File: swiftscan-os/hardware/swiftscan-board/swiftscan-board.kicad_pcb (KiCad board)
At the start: 2 copper layers, 80 x 55 mm, 11 parts, among them J1 I2S_MIC, U1 ATECC608A, U2 VCNL4040

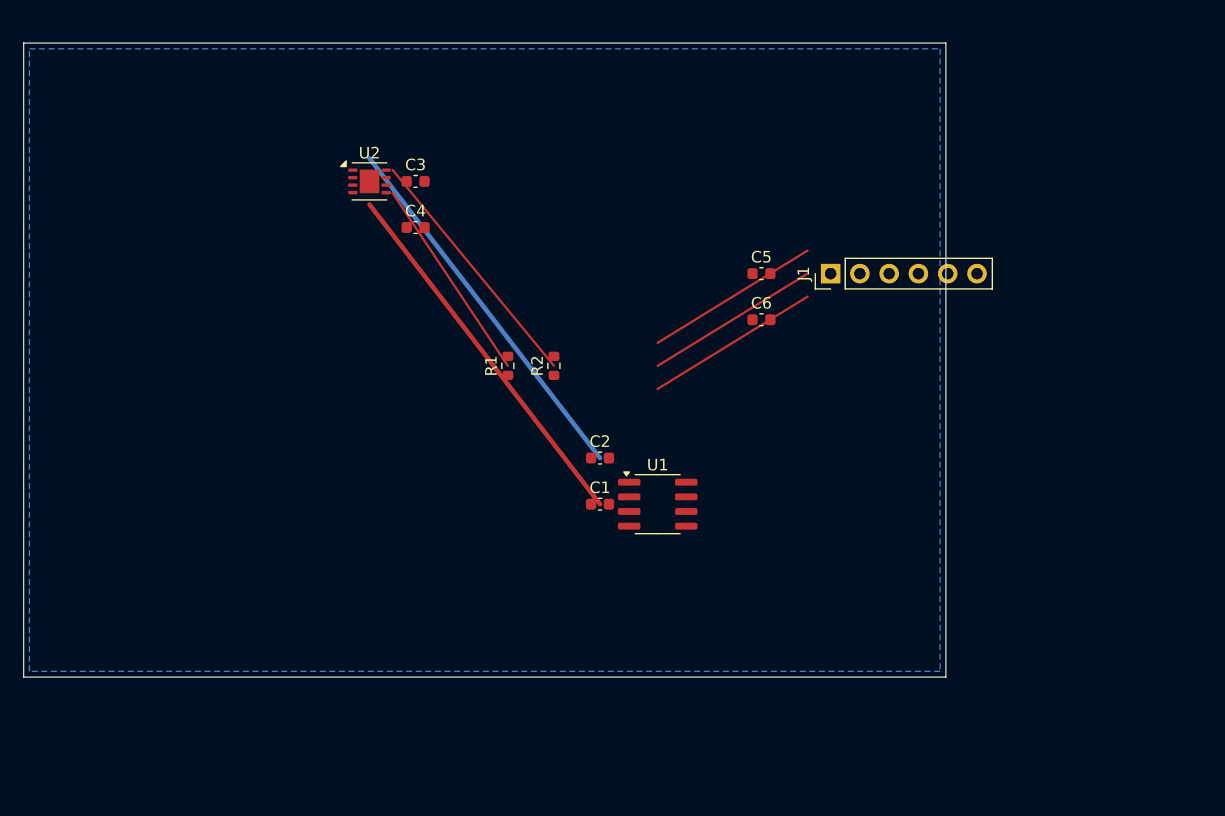
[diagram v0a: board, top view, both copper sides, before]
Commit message: Add fuel gauge, BME280, GPIO header, and mounting holes
Extend the scanning board KiCad package with MAX17048 on VBATT,
BME280 environmental sensing, a 10-pin GPIO breakout, and four
grounded M3 corner holes with clearance rings and updated power rules.

Co-authored-by: James Rallis <jrallis988@users.noreply.github.com>
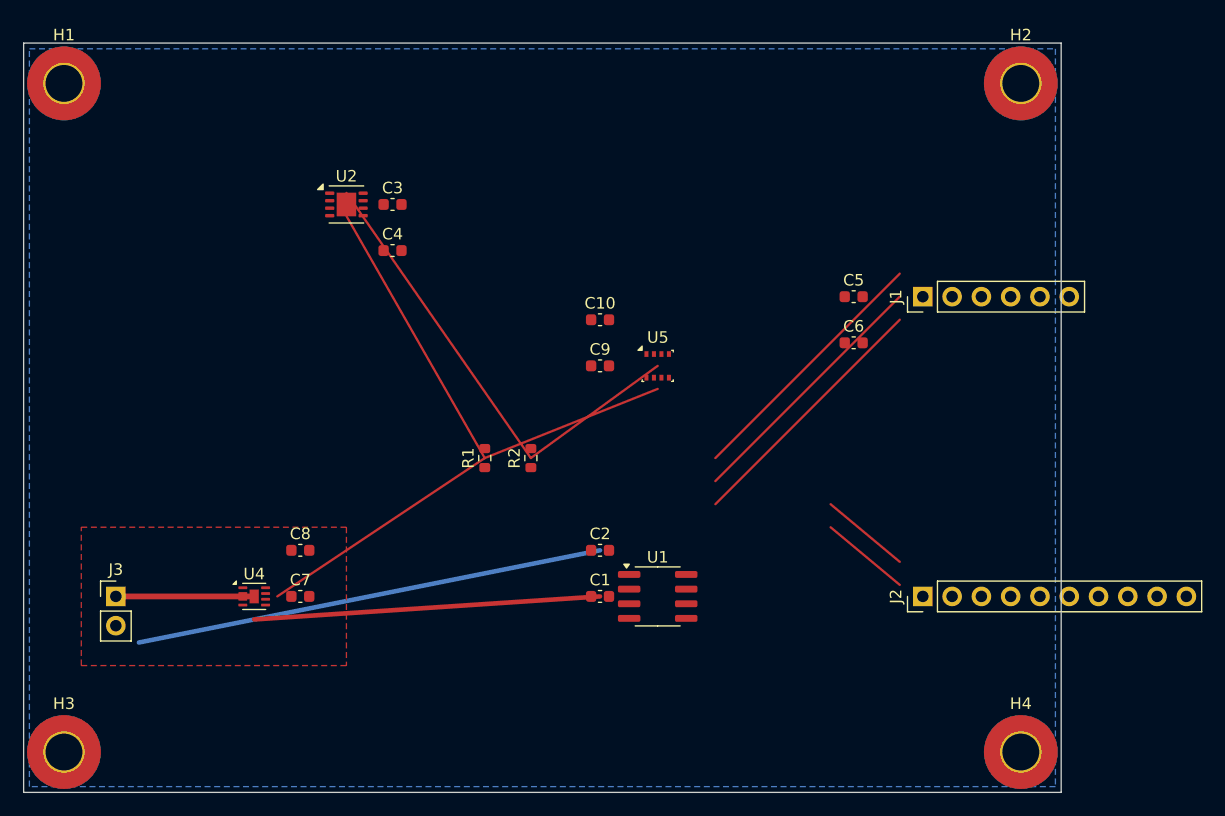
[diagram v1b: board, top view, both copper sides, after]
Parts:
- added C10: 1uF, C_0603_1608Metric, F.Cu at (50.0, 24.0)
- added C7: 100nF, C_0603_1608Metric, F.Cu at (24.0, 48.0)
- added C8: 1uF, C_0603_1608Metric, F.Cu at (24.0, 44.0)
- added C9: 100nF, C_0603_1608Metric, F.Cu at (50.0, 28.0)
- added H1: M3, MountingHole_3.2mm_M3_Pad_TopBottom, F.Cu at (3.50, 3.50)
- added H2: M3, MountingHole_3.2mm_M3_Pad_TopBottom, F.Cu at (86.5, 3.50)
- added H3: M3, MountingHole_3.2mm_M3_Pad_TopBottom, F.Cu at (3.50, 61.5)
- added H4: M3, MountingHole_3.2mm_M3_Pad_TopBottom, F.Cu at (86.5, 61.5)
- added J2: GPIO_BREAKOUT, PinHeader_1x10_P2.54mm_Vertical, F.Cu at (78.0, 48.0)
- added J3: LiPo, PinHeader_1x02_P2.54mm_Vertical, F.Cu at (8.00, 48.0)
- added U4: MAX17048, TDFN-8-1EP_2x2mm_P0.5mm_EP0.8x1.2mm, F.Cu at (20.0, 48.0)
- added U5: BME280, Bosch_LGA-8_2.5x2.5mm_P0.65mm_ClockwisePinNumbering, F.Cu at (55.0, 28.0)
- moved C5 8.25 mm to (72.0, 22.0)
- moved C6 8.25 mm to (72.0, 26.0)
- moved J1 8.25 mm to (78.0, 22.0)
- moved R1 8.25 mm to (40.0, 36.0)
- moved R2 8.25 mm to (44.0, 36.0)
- moved C1 8.00 mm to (50.0, 48.0)
- moved C2 8.00 mm to (50.0, 44.0)
- moved U1 8.00 mm to (55.0, 48.0)
- moved C3 2.83 mm to (32.0, 14.0)
- moved C4 2.83 mm to (32.0, 18.0)
- moved U2 2.83 mm to (28.0, 14.0)
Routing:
- net I2C_SDA: track 18.0 -> 62.0 mm
- net I2S_DIN: track 0.00 -> 22.6 mm
- net I2S_BCLK: track 0.00 -> 22.6 mm
- net GND: track 63.3 -> 40.8 mm
- net I2C_SCL: track 22.0 -> 41.6 mm
- net VBATT: track 0.00 -> 12.0 mm
- net GPIO2: track 0.00 -> 7.81 mm
- net GPIO1: track 0.00 -> 7.81 mm
- net I2S_WS: track 15.3 -> 22.6 mm
- net +3V3: track 32.8 -> 30.1 mm
- added copper zone on F.Cu, net VBATT
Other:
- board size 80 x 55 mm -> 90 x 65 mm
- board text added: "BME280"
- board text added: "GPIO J2"
- board text added: "I2S MIC"
- board text added: "M3 GND holes + 4mm clearance rings"
- board text added: "MAX17048 / LiPo"
- board text added: "VCNL4040"
- board text added: "clr 0.15mm sig / 0.20mm 3V3 / 0.25mm VBATT"
- board text removed: "I2S MIC HDR"
- board text removed: "VCNL4040 near camera"
- board text removed: "clr 0.15mm sig / 0.20mm pwr; decap<=2mm"
